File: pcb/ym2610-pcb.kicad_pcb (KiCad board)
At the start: 4 copper layers, 100.9 x 77.5 mm, 132 parts, among them J1 MIDI_IN, J2 LINE_OUT, J3 HEADPHONES, J4 SPDIF_COAX, J5 UART, SW1 BTN_A, SW2 BTN_B, SW3 CRESET, U1 YM2610, U10 TSV914IPT, U11 TSV914IPT, U12 AD8532, U13 74LVC2G08, U14 74AHCT595, U15 74AHCT595, U16 SPDIF_OPTICAL, U17 74HCT573, U18 TLP2361, U19 74HCT153, U2 YM3016, U20 74HCT153, U21 74LVC257, U3 74LV1T34, U4 74LVC244, U5 74LV1T34, U6 74HCT573, U7 74HCT573, U8 74HCT153, U9 74HCT153

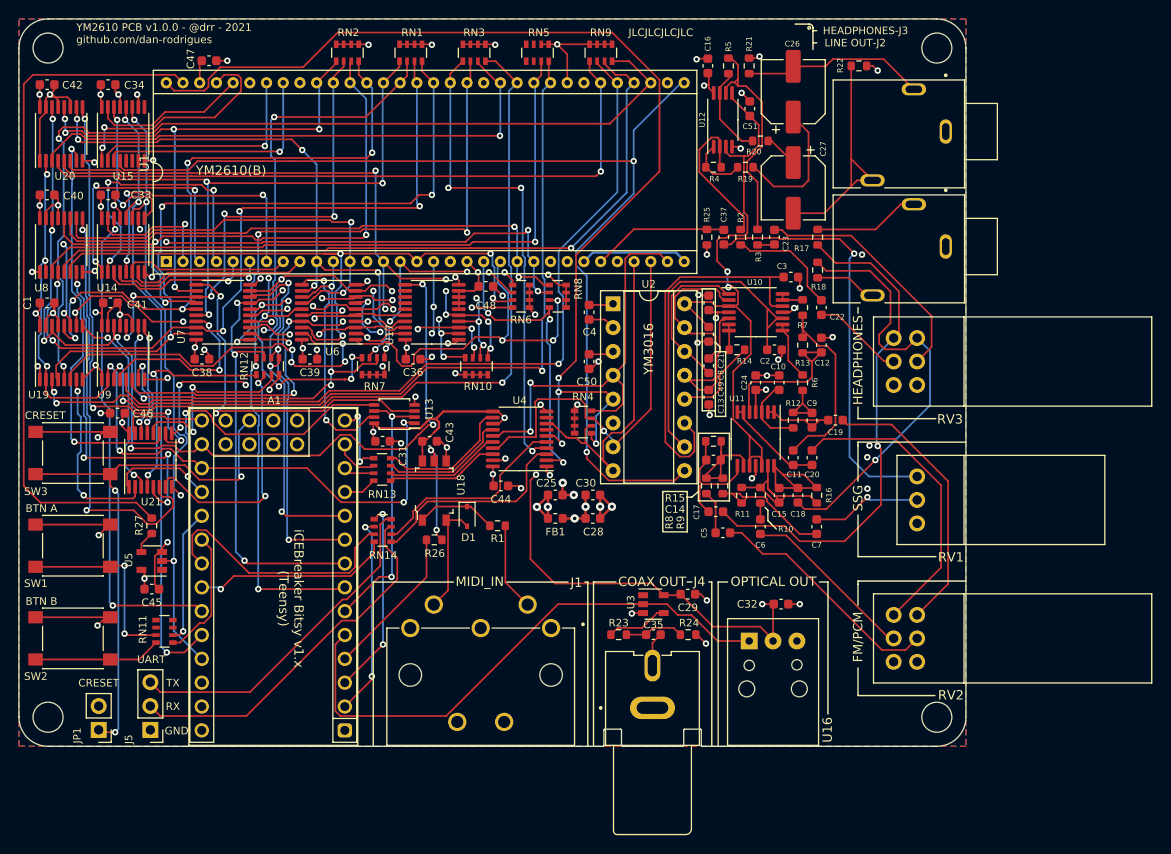
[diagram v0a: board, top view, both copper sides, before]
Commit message: pcb: bump version from v1.0.0 to tentative v1.0.1a
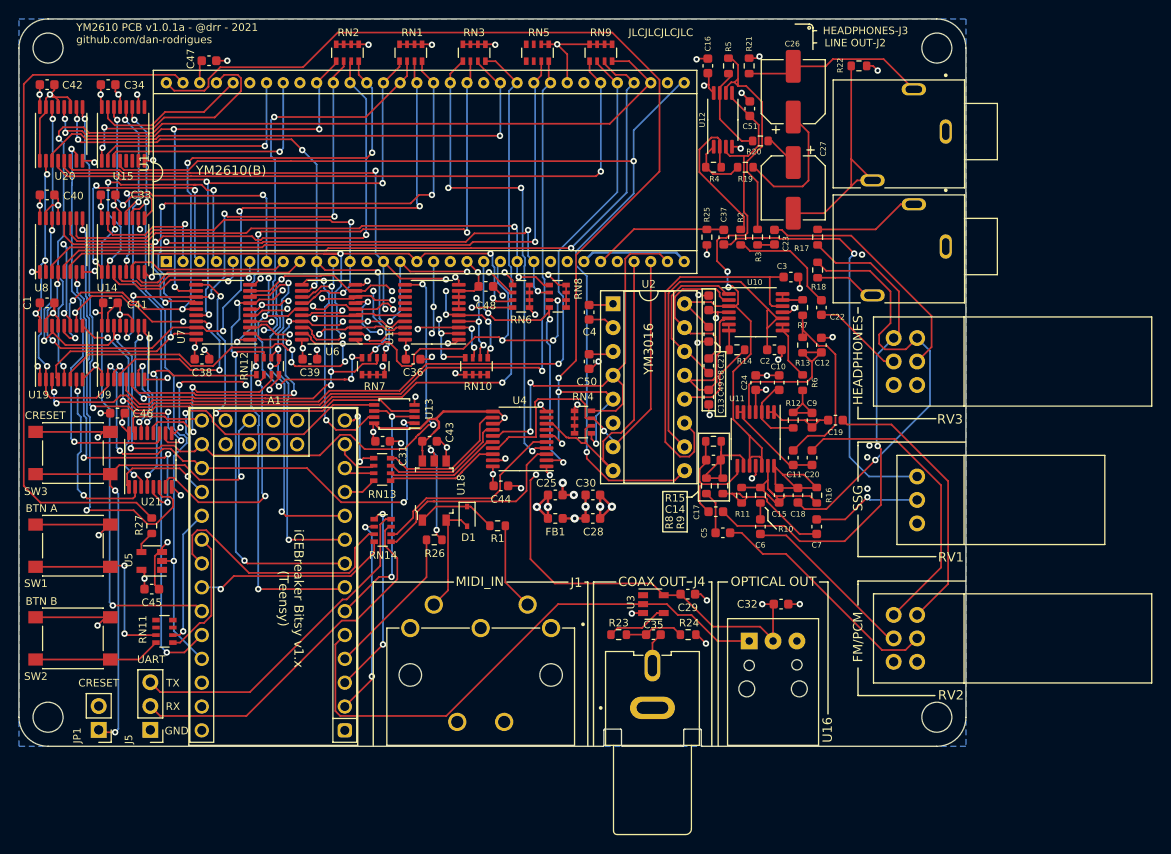
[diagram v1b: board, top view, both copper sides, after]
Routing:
- removed copper zone on F.Cu, net GND
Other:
- board text added: "YM2610 PCB v1.0.1a - @drr - 2021 github.com/dan-rodrigues"
- board text removed: "YM2610 PCB v1.0.0 - @drr - 2021 github.com/dan-rodrigues"

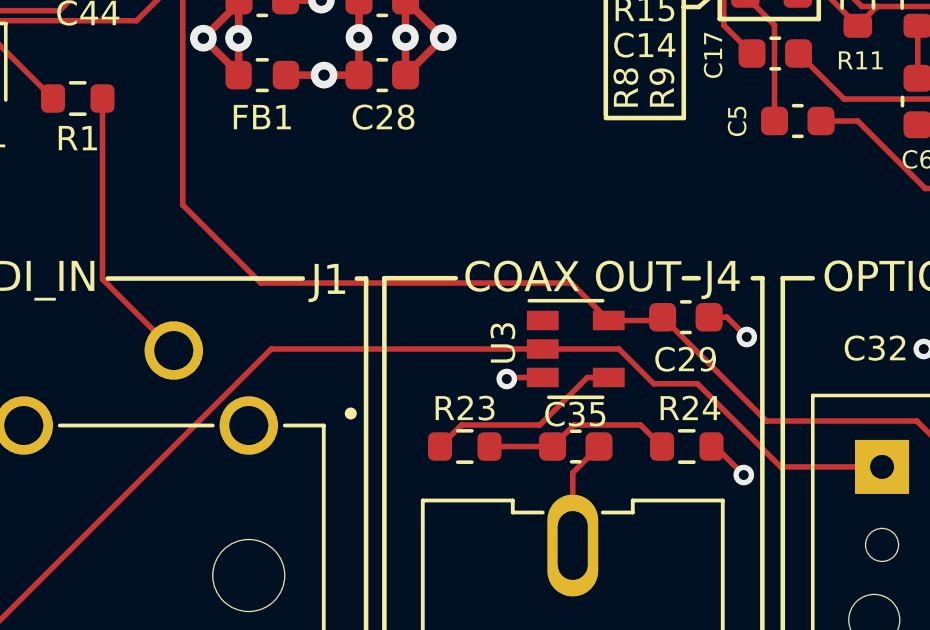
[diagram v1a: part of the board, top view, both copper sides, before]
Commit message: pcb: replace LV1T34 with LVC1G34 as S/PDIF coax buffer
The earlier design used the LVC part but to remove a unique item from BOM, it was replaced with another LV1 part. This was a mistake as the LV1T34 can't quite drive the coax load (vs. 24mA on the LVC1G34).
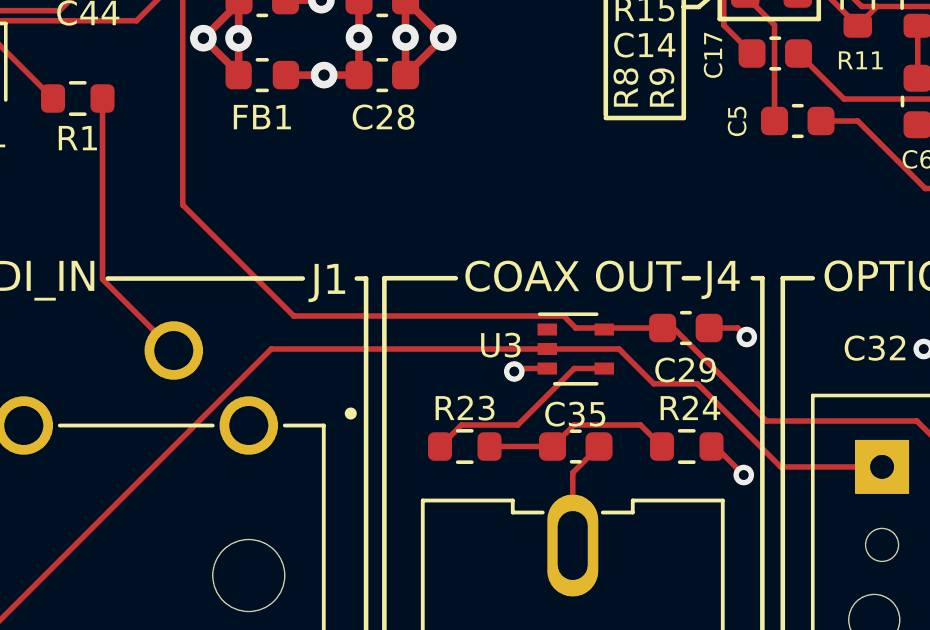
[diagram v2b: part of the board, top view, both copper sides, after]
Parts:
- U3: value 74LV1T34 -> 74LVC1G34; footprint Package_TO_SOT_SMD:SOT-23-5 -> Package_TO_SOT_SMD:SOT-353_SC-70-5
- moved C29 0.36 mm to (88.8, 107.9)

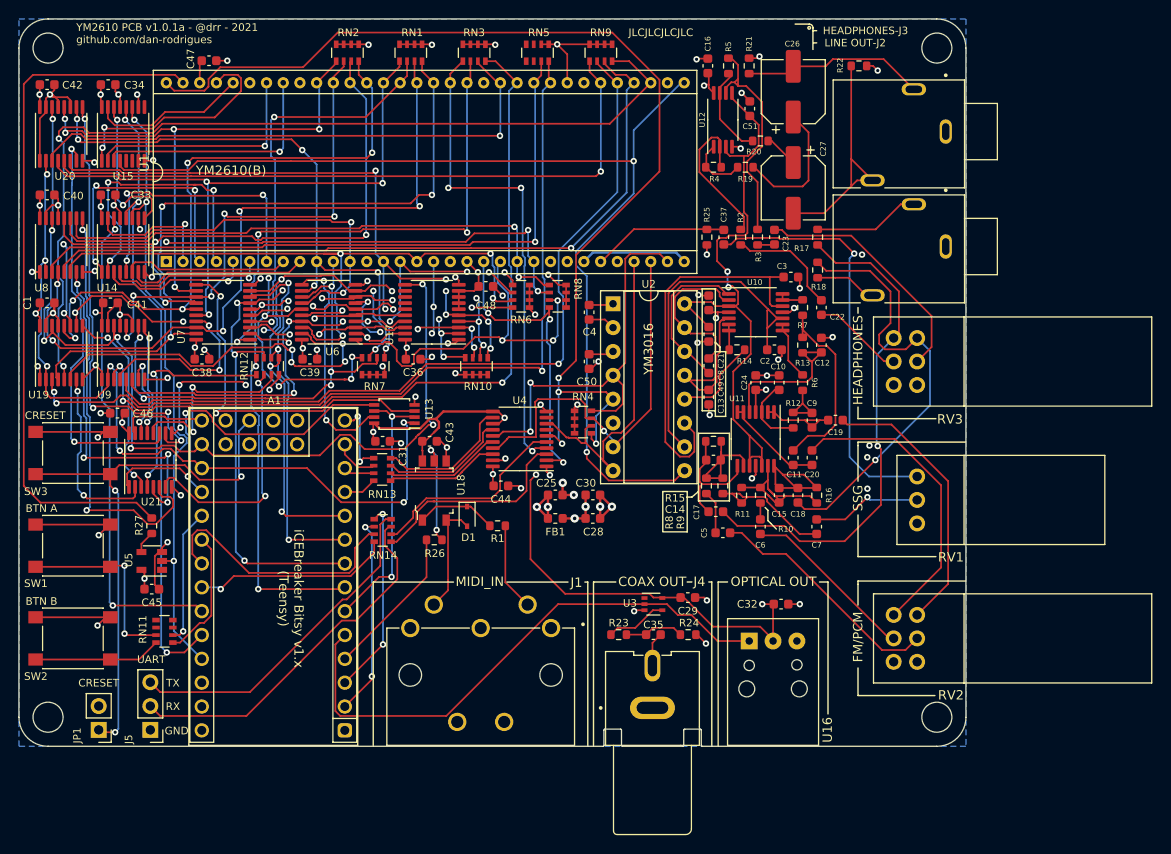
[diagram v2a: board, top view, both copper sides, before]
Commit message: pcb: misc. cleanup in analog section
* added net-tie and dedicated return for headphone to avoid running over much of the DAC circuit
* route SSG on back layer
* ground fill on top
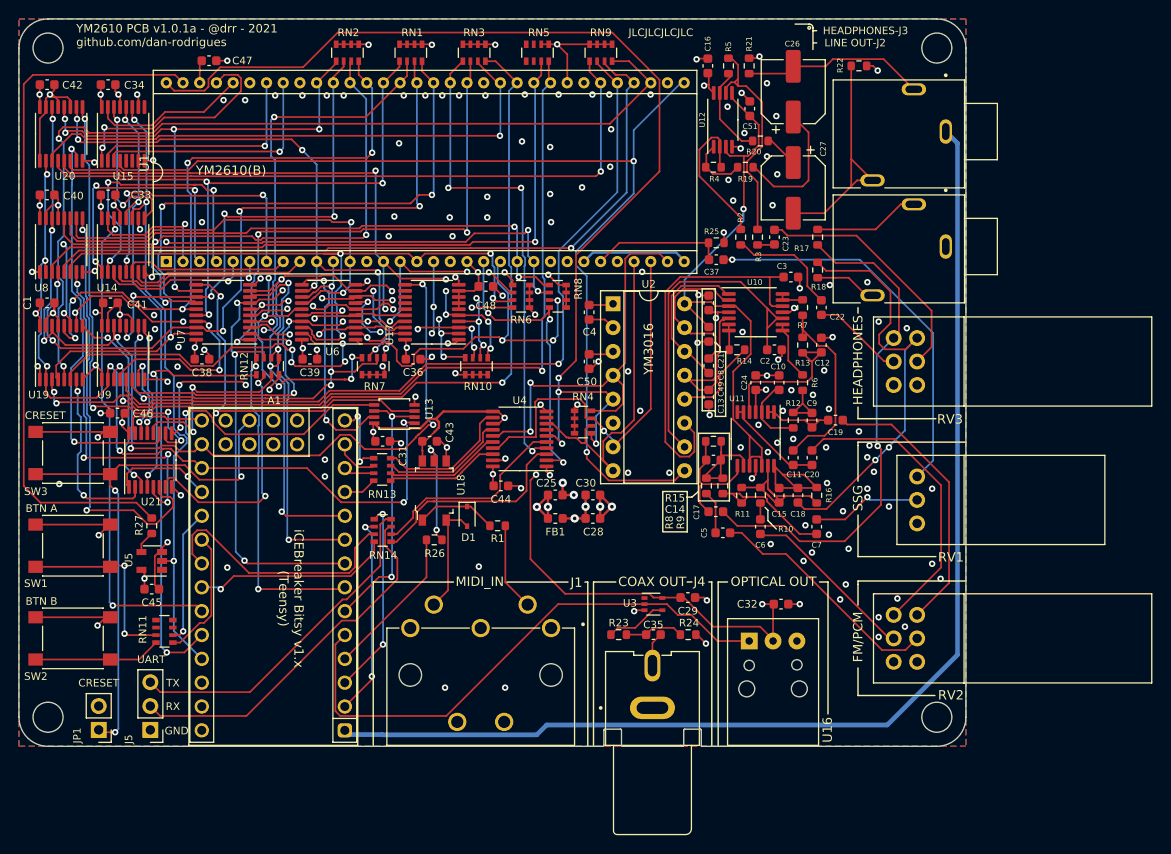
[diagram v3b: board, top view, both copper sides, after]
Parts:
- added NT1: HEADPHONE_RETURN, NetTie:NetTie-2_SMD_Pad0.5mm, B.Cu at (55.7, 122.5)
- moved C37 2.53 mm to (91.8, 71.9), turned to 0 degrees
- moved R25 1.17 mm to (91.8, 70.1), turned to 0 degrees
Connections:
- J3 pad 1: GND -> Net-(J3-Pad1)
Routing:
- net Net-(J3-Pad1): track 0.00 -> 121.1 mm
- net GND: track 159.9 -> 163.2 mm, vias 64 -> 156
- net /SSG: track 44.8 -> 41.6 mm
- net /RB_2V5: track 66.9 -> 65.0 mm, vias 2 -> 1
- net /LINE_R: track 46.6 -> 45.5 mm, vias 1 -> 2
- net Net-(C37-Pad1): track 14.9 -> 14.1 mm
- added copper zone on F.Cu, net GND

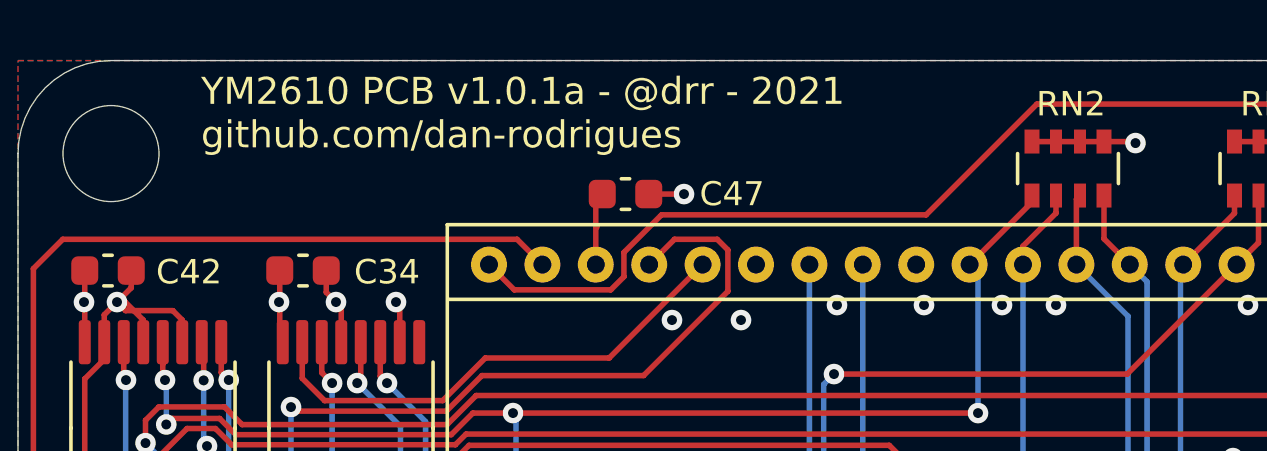
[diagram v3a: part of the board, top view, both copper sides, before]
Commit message: pcb / sch: added CERL-OHL license
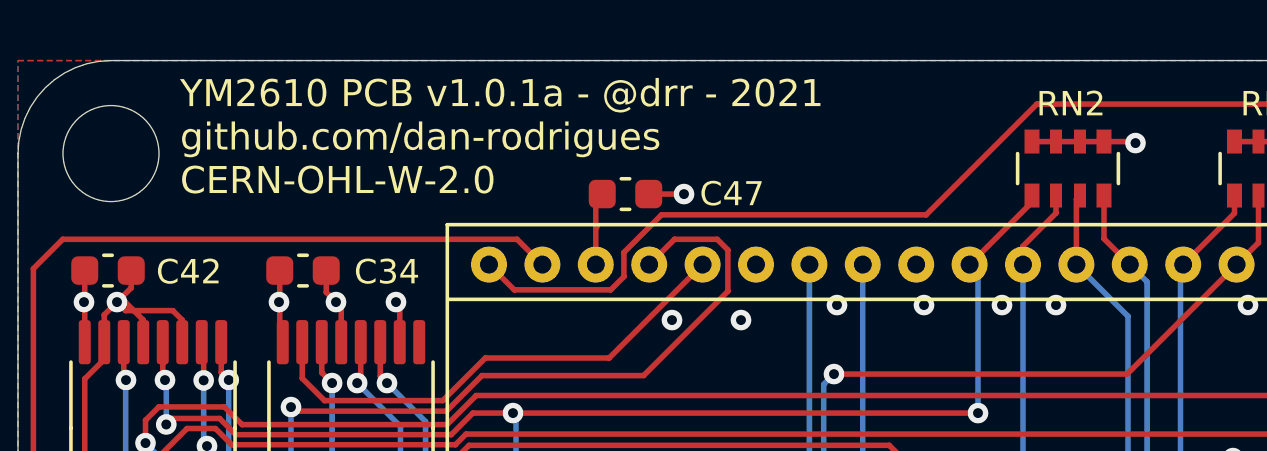
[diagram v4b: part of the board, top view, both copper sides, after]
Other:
- board text added: "YM2610 PCB v1.0.1a - @drr - 2021 github.com/dan-rodrigues CERN-OHL-W-2.0"
- board text removed: "YM2610 PCB v1.0.1a - @drr - 2021 github.com/dan-rodrigues"

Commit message: pcb: tentative v1.0.1
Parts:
- added C52: 150uF, Capacitor_SMD:CP_Elec_5x5.8, F.Cu at (85.0, 100.0)
- added NT2: DAC_CAP_NT, NetTie:NetTie-2_SMD_Pad0.5mm, B.Cu at (82.3, 80.2)
- added R28: 100R, Resistor_SMD:R_0603_1608Metric, F.Cu at (81.2, 100.2)
- added R29: 100R, Resistor_SMD:R_0603_1608Metric, F.Cu at (77.7, 86.8)
- added R30: 100R, Resistor_SMD:R_0603_1608Metric, F.Cu at (77.7, 84.3)
- added R31: 100R, Resistor_SMD:R_0603_1608Metric, F.Cu at (77.7, 94.4)
- added R32: 100R, Resistor_SMD:R_0603_1608Metric, F.Cu at (77.7, 91.8)
- R21, R22: value 50k -> 47k
- moved NT1 51.2 mm to (82.8, 79.1)
- moved R22 18.1 mm to (95.6, 65.4), turned to 270 degrees
- moved RN4 9.11 mm to (70.7, 83.2), turned to 270 degrees
- moved C23 6.78 mm to (91.7, 67.0), turned to 180 degrees
- moved R3 6.22 mm to (91.7, 65.2), turned to 0 degrees
- moved C50 2.06 mm to (78.4, 80.7), turned to 270 degrees
- moved C4 0.15 mm to (78.4, 77.5)
- moved R2 0.15 mm to (94.4, 69.3)
- turned C51 to 90 degrees
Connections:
- C4 pad 2: +5VA -> /DAC_5V
- C50 pad 2: +5VA -> /DAC_5V
- RN4 pad 1: +5VA -> +5V
- RN4 pad 2: +5VA -> +5V
- RN4 pad 3: +5VA -> +5V
- RN4 pad 4: +5VA -> +5V
- U2 pad 1: +5VA -> /DAC_5V
- U2 pad 3: +5VA -> /DAC_5V
- U2 pad 4: /DAC_SO -> Net-(R30-Pad1)
- U2 pad 5: /DAC_CLK -> Net-(R29-Pad1)
- U2 pad 6: +5VA -> /DAC_5V
- U2 pad 7: /DAC_SH2 -> Net-(R32-Pad1)
- U2 pad 8: /DAC_SH1 -> Net-(R31-Pad1)
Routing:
- net /DAC_5V: track 0.00 -> 39.0 mm, vias 0 -> 1
- net Net-(C52-Pad2): track 0.00 -> 23.2 mm, vias 0 -> 1
- net Net-(J3-Pad1): track 121.1 -> 100.3 mm
- net Net-(C27-Pad2): track 25.1 -> 13.8 mm
- net Net-(C23-Pad2): track 26.4 -> 34.1 mm
- net /DAC_SO: track 44.0 -> 36.4 mm
- net /DAC_SH1: track 36.1 -> 43.3 mm, vias 0 -> 4
- net /DAC_SH2: track 42.2 -> 48.6 mm, vias 1 -> 4
- net Net-(C26-Pad1): track 14.0 -> 7.94 mm, vias 0 -> 2
- net +5VA: track 22.7 -> 18.3 mm, vias 6 -> 5
- net /DAC_CLK: track 116.3 -> 111.9 mm, vias 4 -> 3
- net GND: track 163.2 -> 167.1 mm, vias 156 -> 165
- net +5V: track 84.8 -> 88.3 mm, vias 23 -> 24
- net Net-(R31-Pad1): track 0.00 -> 2.33 mm
- net Net-(R30-Pad1): track 0.00 -> 2.31 mm
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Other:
- board text added: "MIDI IN"
- board text added: "YM2610 PCB v1.0.1 - @drr - 2021 github.com/dan-rodrigues CERN-OHL-W-2.0"
- board text removed: "YM2610 PCB v1.0.1a - @drr - 2021 github.com/dan-rodrigues CERN-OHL-W-2.0"
